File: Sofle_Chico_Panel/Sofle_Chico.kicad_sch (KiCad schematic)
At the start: 115 parts, among them J1 Conn_01x05, J2 MJ-4PP-9, J3 Conn_01x04, J4 Conn_01x04, J5 Conn_01x05, J6 Conn_01x05, J7 Conn_01x04, Q1 Si2301CDS, SW1 SW_PUSH, SW10 SW_PUSH, SW11 SW_PUSH, SW12 SW_PUSH, SW13 SW_PUSH, SW14 SW_PUSH, SW15 SW_PUSH, SW16 SW_PUSH, SW17 SW_PUSH, SW18 SW_PUSH, SW19 SW_PUSH, SW2 SW_PUSH, SW20 SW_PUSH, SW21 SW_PUSH, SW22 SW_PUSH, SW23 SW_PUSH, SW24 SW_PUSH, SW25 Rotary_Encoder_Switch-Device, SW26 SW_PUSH, SW27 SW_PUSH, SW28 SW_PUSH, SW29 SW_PUSH, SW3 SW_PUSH, SW30 SW_PUSH, SW4 SW_PUSH, SW5 SW_PUSH, SW6 SW_PUSH, SW7 SW_PUSH, SW8 SW_PUSH, SW9 SW_PUSH, U1 74LVC1G34SE-7, U2 Pico

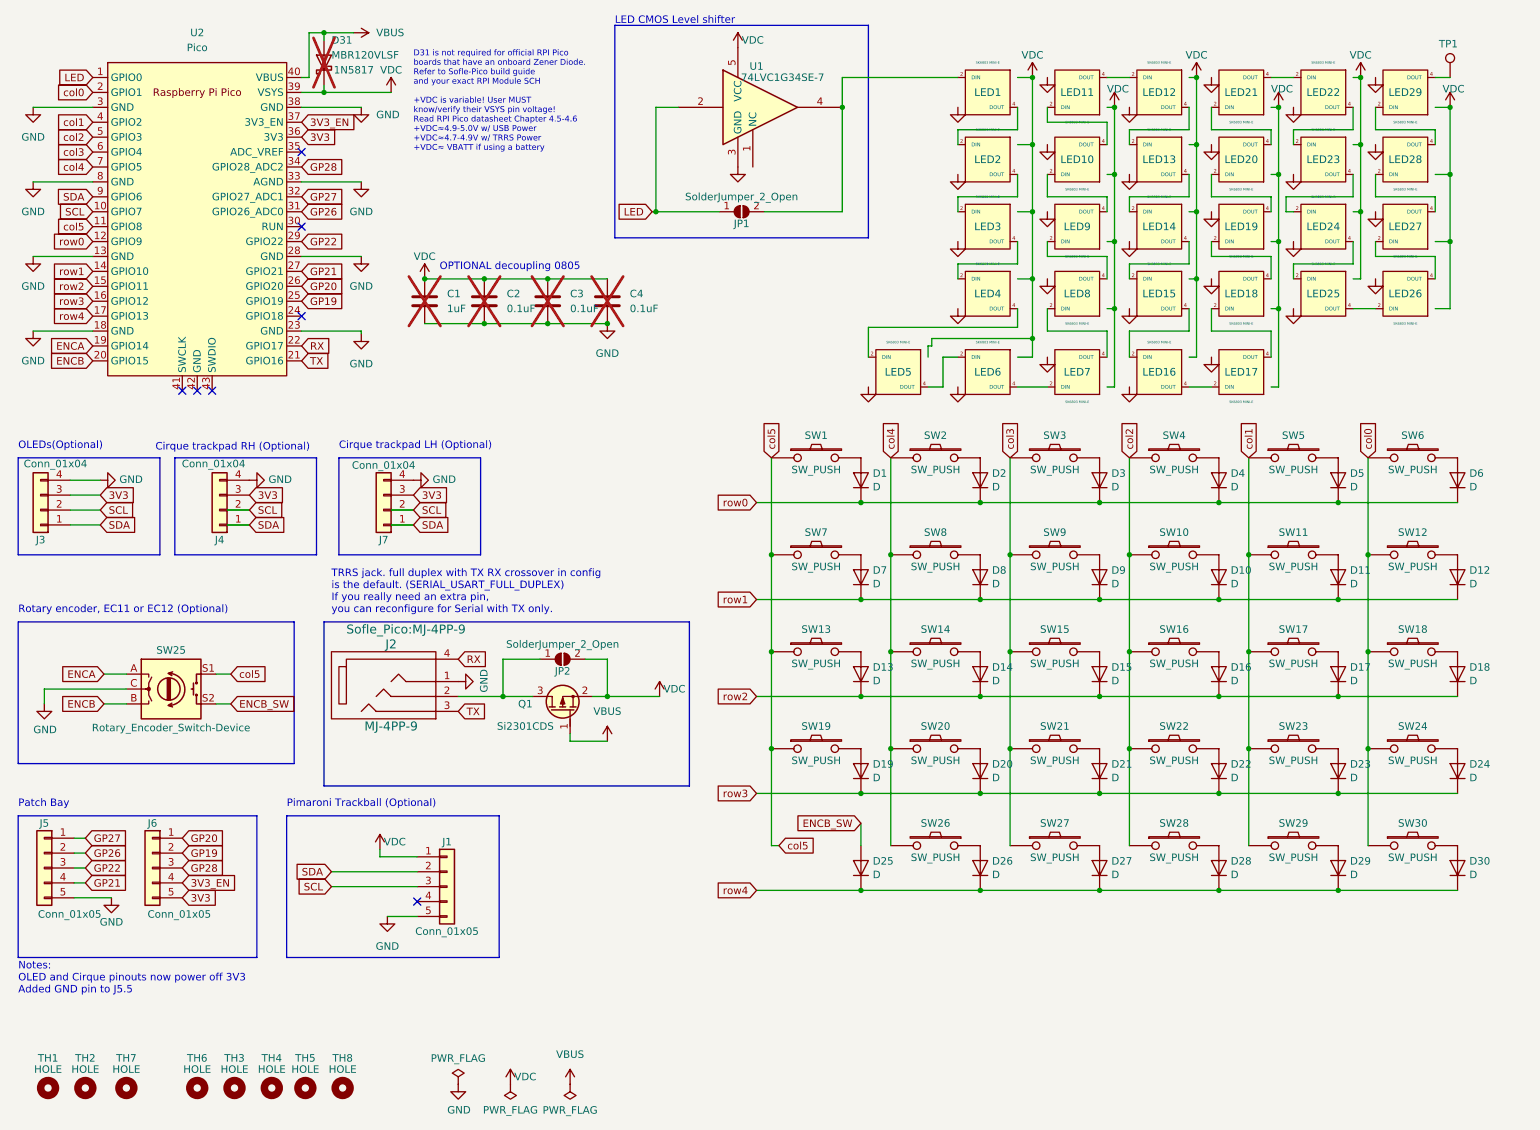
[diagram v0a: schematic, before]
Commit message: panelized Chico and Pico, ordered turnkey single-sided JLCPCB per this rev
$35.43 for 5 Pico boards assembled
$35.43 for 5 Chico boards assembled
$55.95 shipping
$7.04 tax
-$10 newbie coupon
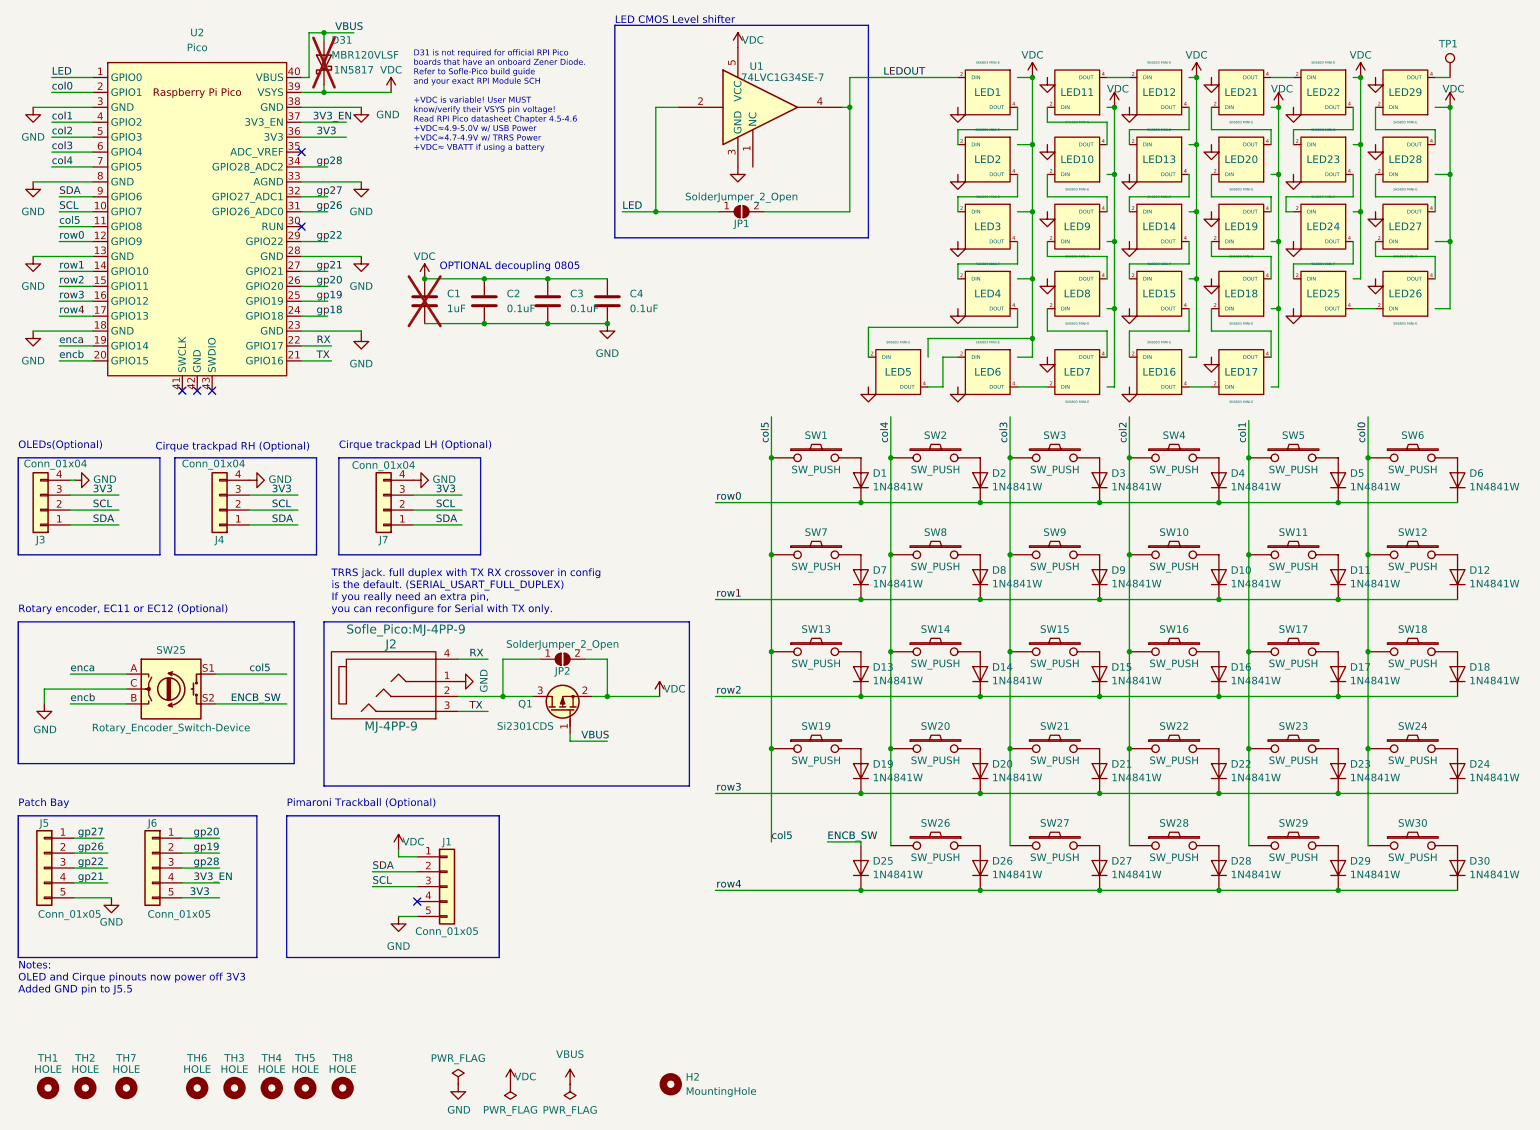
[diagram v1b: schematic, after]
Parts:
- added H2: MountingHole, Sofle_Pico:JLC_SMT_TOOLING_HOLE_1.152MM, symbol Mechanical:MountingHole
- C1:  LCSC part number (none) -> C49678
- C2, C3, C4:  LCSC part number (none) -> C81598; now fitted; now in the parts list
- D1, D10, D11, D12, D13, D14, D15, D16, D17, D18, D19, D2, D20, D21, D22, D23, D24, D25, D26, D27, D28, D29, D3, D30, D4, D5, D6, D7, D8, D9: value D -> 1N4841W;  LCSC part number (none) -> C94111
- D31: MFG PN (none) -> MBR120VLSF; now left out of the parts list
- Q1:  LCSC part number (none) -> C28323; MFG (none) -> VISHAY; MFG PN (none) -> Si2301CDS
- U1: JLCPCB_PN (none) -> C94111; MFG (none) -> Diodes Inc / TI; MFG PN (none) -> 74LVC1G34SE-7; Mfg Diodes Inc / TI -> (none)
- U2:  LCSC part number (none) -> C10487
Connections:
- net LEDOUT: now reaches JP1.2 (B), LED1.2 (DIN), U1.4
- net gp18: now reaches U2.24 (GPIO18)
- net ENCA renamed enca
- net ENCB renamed encb
- net GP19 renamed gp19
- net GP20 renamed gp20
- net GP21 renamed gp21
- net GP22 renamed gp22
- net GP26 renamed gp26
- net GP27 renamed gp27
- net GP28 renamed gp28
- no-connect marks 7 -> 6

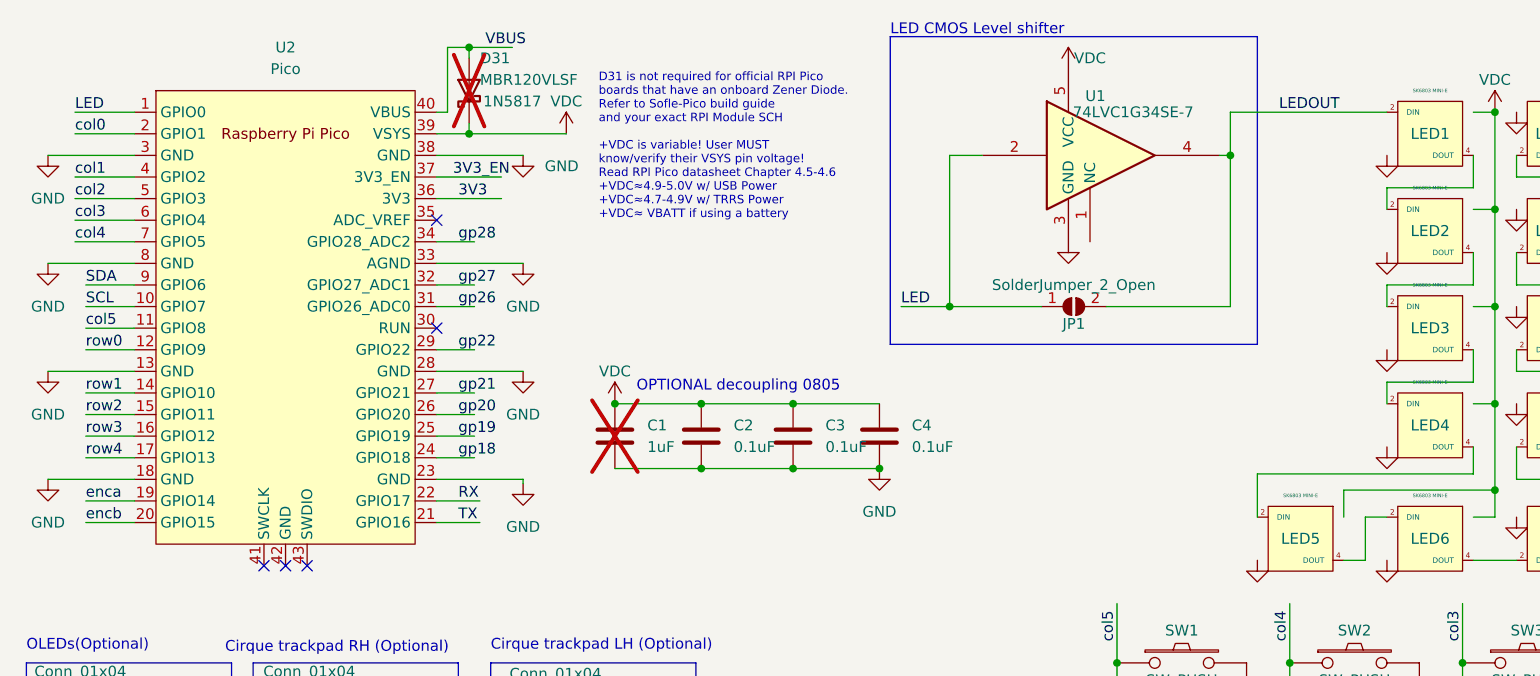
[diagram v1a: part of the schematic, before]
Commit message: Reworked as "batwing" with single-controller connections and no mid-slot to sneak it past JLCPCB.  Singulating will be manual, but lets you get 5 boards with diodes preinstalled
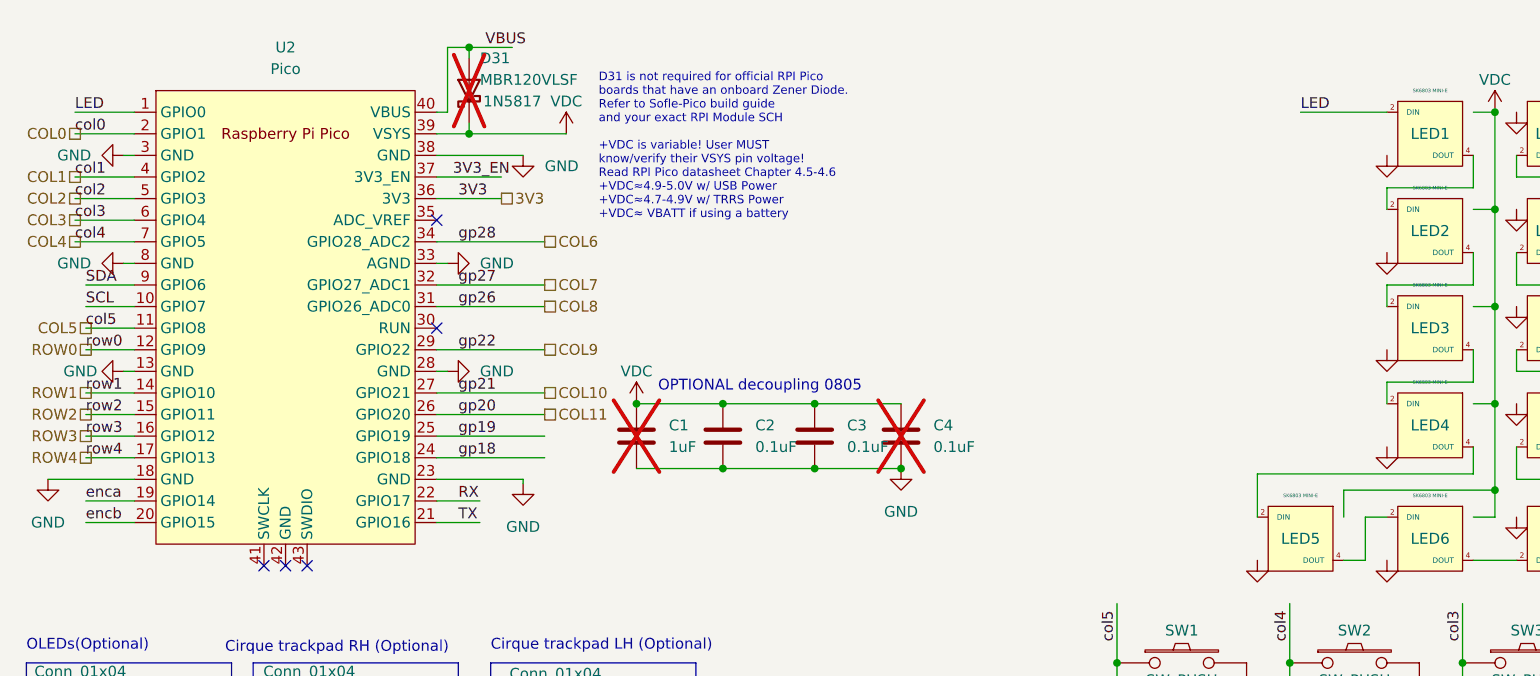
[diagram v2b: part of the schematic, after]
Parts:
- removed JP1: SolderJumper_2_Open, Sofle_Pico:Level Shifter Bypass Jumper, symbol Sofle_Pico:SolderJumper_2_Open
- removed U1: 74LVC1G34SE-7, Package_TO_SOT_SMD:SOT-353_SC-70-5_Handsoldering, symbol 74xGxx:74LVC1G34
- C4: now not fitted; now left out of the parts list
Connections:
- net LEDOUT is gone; now on net LED: LED1.2 (DIN)
- net col0 renamed COL0
- net col1 renamed COL1
- net col2 renamed COL2
- net col3 renamed COL3
- net col4 renamed COL4
- net col5 renamed COL5
- net gp20 renamed COL11
- net gp21 renamed COL10
- net gp22 renamed COL9
- net gp26 renamed COL8
- net gp27 renamed COL7
- net gp28 renamed COL6
- net row0 renamed ROW0
- net row1 renamed ROW1
- net row2 renamed ROW2
- net row3 renamed ROW3
- net row4 renamed ROW4
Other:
- note removed: "LED CMOS Level shifter"
- moved on the sheet: C1, C2, C3
